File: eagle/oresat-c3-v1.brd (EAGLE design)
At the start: 99.8 x 94.7 mm, 174 parts, among them J1 J-SAMTEC-TFM-110-X1-XXX-D-RA, J10 U.FL, J11 U.FL, J13 U.FL, J14 U.FL, J15 HARWIN-2X8X1.27, J19 HARWIN-2X8X1.27, J2 U.FL, J3 U.FL, J4 U.FL, J6 J-SAMTEC-TFM-120-X1-XXX-D-RA, J7 FTSH-105-XX-X-DV-K, J8 U.FL, J9 U.FL, Q1 MOSFET-PCH-SOT23-6, U1 MAX892LEUA+T21-0036K-L, U11 U-ONSEMI-AX5043, U12 LP2985XX-N, U13 U-ONSEMI-AX5043, U14 LP2985XX-N, U2 TCAN330, U3 TCAN330, U4 TPS259621 - eFuse, U5 TPS62111RSA, U6 MAX6374KA-T21-0078H-L, U7 STM32F446RE, U9 SFEM016GB1EM1TO-A-HG-111-STD, X1 16MHZ-2.5x2mm, X3 TAITIEN-TY, X4 TAITIEN-TY

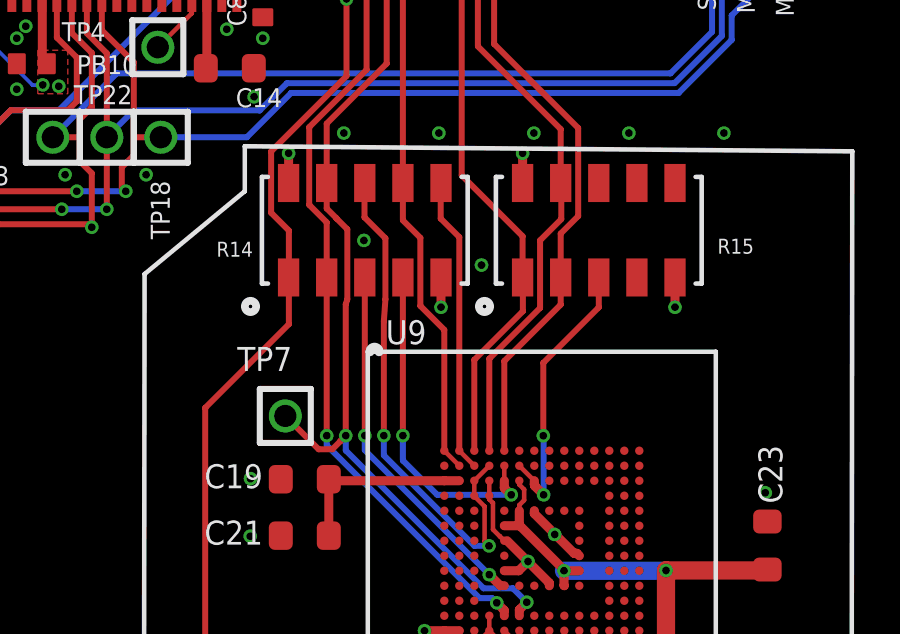
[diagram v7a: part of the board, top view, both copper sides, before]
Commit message: Fix net error
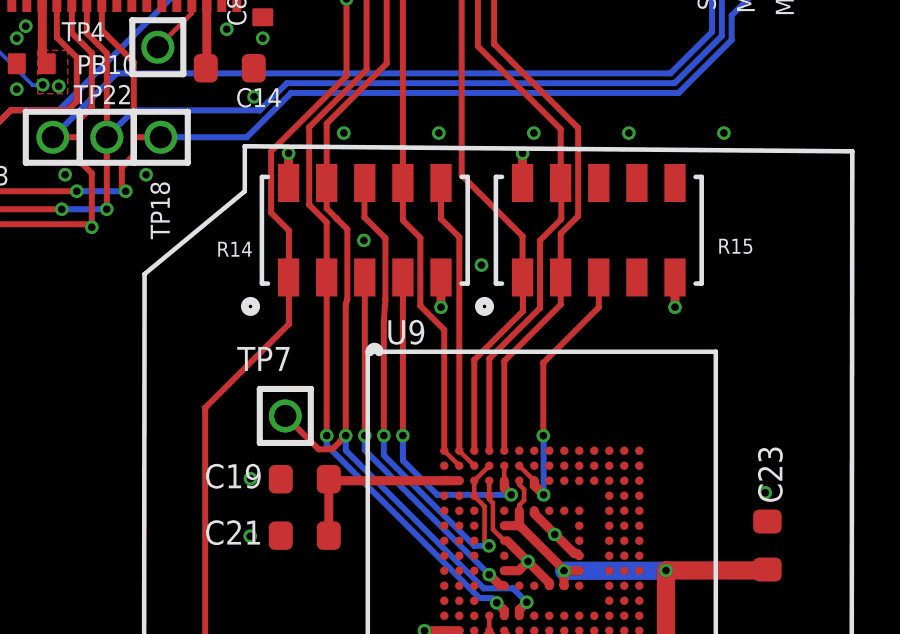
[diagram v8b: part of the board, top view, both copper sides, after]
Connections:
- removed net N$4: R14.6
- net SDIO_D4: now also R14.6
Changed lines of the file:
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@@
 <wire x1="89.000003125" y1="63.42999375" x2="89.8" y2="63.43" width="0" layer="19" extent="1-1"/>
 <wire x1="88.1" y1="58.88" x2="88.1" y2="60.28" width="0" layer="19" extent="1-1"/>
-<wire x1="84.8" y1="55.93" x2="88.1" y2="57.98" width="0" layer="19" extent="1-1"/>
-<wire x1="84.75" y1="55.88" x2="84.8" y2="55.93" width="0" layer="19" extent="1-1"/>
-<wire x1="82.3" y1="54.83" x2="83.7" y2="54.83" width="0" layer="19" extent="1-1"/>
-<wire x1="79.85" y1="56.38" x2="80.7" y2="55.98" width="0" layer="19" extent="1-1"/>
-<wire x1="79.85" y1="56.98" x2="79.85" y2="56.38" width="0" layer="19" extent="1-1"/>
-<wire x1="79.85" y1="57.58" x2="79.85" y2="56.98" width="0" layer="19" extent="1-1"/>
-<wire x1="79.85" y1="58.18" x2="79.85" y2="57.58" width="0" layer="19" extent="1-1"/>
-<wire x1="80.7" y1="58.18" x2="79.85" y2="58.18" width="0" layer="19" extent="1-1"/>
-<wire x1="80.7" y1="57.08" x2="79.85" y2="56.98" width="0" layer="19" extent="1-1"/>
-<wire x1="60.03" y1="55.85" x2="78.8" y2="56.98" width="0" layer="19" extent="1-1"/>
-<wire x1="59.95" y1="55.19" x2="60.03" y2="55.85" width="0" layer="19" extent="1-1"/>
-<wire x1="59.3" y1="55.2" x2="59.95" y2="55.19" width="0" layer="19" extent="1-1"/>
-<wire x1="59.585" y1="54.625" x2="59.3" y2="55.2" width="0" layer="19" extent="1-1"/>
-<wire x1="59.3" y1="55.9" x2="59.3" y2="55.2" width="0" layer="19" extent="1-1"/>
-<wire x1="58.6" y1="46" x2="59.585" y2="54.625" width="0" layer="19" extent="1-1"/>
-<wire x1="59.46" y1="39.7654" x2="58.674" y2="45.212" width="0" layer="19" extent="1-1"/>
-<wire x1="64.54" y1="35.6252" x2="59.46" y2="38.7748" width="0" layer="19" extent="1-1"/>
-<wire x1="67.26" y1="38.7748" x2="64.54" y2="35.6252" width="0" layer="19" extent="1-1"/>
-<wire x1="72.32" y1="35.64380625" x2="67.26" y2="38.7748" width="0" layer="19" extent="1-1"/>
-<wire x1="72.34" y1="35.6252" x2="72.332934375" y2="35.630871875" width="0" layer="19" extent="1-1"/>
-<wire x1="51.235" y1="45.275" x2="57.735" y2="45.275" width="0" layer="19" extent="1-1"/>
-<wire x1="51.265" y1="42.045" x2="51.4" y2="42.75" width="0" layer="19" extent="1-1"/>
-<wire x1="32.5" y1="65.1" x2="32.5" y2="65.6" width="0" layer="19" extent="1-1"/>
-<wire x1="32" y1="65.6" x2="32.5" y2="65.6" width="0" layer="19" extent="1-1"/>
-<wire x1="31.5" y1="65.6" x2="32" y2="65.6" width="0" layer="19" extent="1-1"/>
-<wire x1="31.5" y1="65.1" x2="31.5" y2="65.6" width="0" layer="19" extent="1-1"/>
-<wire x1="31" y1="65.1" x2="31.5" y2="65.1" width="0" layer="19" extent="1-1"/>
-<wire x1="31" y1="65.6" x2="31.5" y2="65.6" width="0" layer="19" extent="1-1"/>
-<wire x1="32" y1="65.1" x2="32.5" y2="65.1" width="0" layer="19" extent="1-1"/>
-<wire x1="51.8" y1="42" x2="51.265" y2="42.045" width="0" layer="19" extent="1-1"/>
-<wire x1="47.7" y1="55.5" x2="47.4" y2="54.864" width="0" layer="19" extent="1-1"/>
-<wire x1="48.385" y1="54.625" x2="47.4" y2="54.864" width="0" layer="19" extent="1-1"/>
-<wire x1="48.7" y1="55.2" x2="48.385" y2="54.625" width="0" layer="19" extent="1-1"/>
-<wire x1="32" y1="66.7" x2="32" y2="65.6" width="0" layer="19" extent="1-1"/>
-<wire x1="49.54" y1="56.16" x2="48.7" y2="55.2" width="0" layer="19" extent="1-1"/>
-<wire x1="50.235" y1="56.475" x2="49.54" y2="56.16" width="0" layer="19" extent="1-1"/>
-<wire x1="49.37" y1="57.05" x2="49.54" y2="56.16" width="0" layer="19" extent="1-1"/>
-<wire x1="49.911" y1="57.4" x2="49.37" y2="57.05" width="0" layer="19" extent="1-1"/>
-<wire x1="28.7" y1="65.425" x2="31" y2="65.1" width="0" layer="19" extent="1-1"/>
-<wire x1="26.725" y1="72.625" x2="28.7" y2="65.425" width="0" layer="19" extent="1-1"/>
-<wire x1="25.7" y1="72.65" x2="25.725" y2="72.625" width="0" layer="19" extent="1-1"/>
-<wire x1="21" y1="77.4" x2="25.7" y2="72.65" width="0" layer="19" extent="1-1"/>
-<wire x1="18.9" y1="72" x2="19.1" y2="77.4" width="0" layer="19" extent="1-1"/>
-<wire x1="57.5" y1="70.825" x2="50.4" y2="66.3" width="0" layer="19" extent="1-1"/>
-<wire x1="59.617" y1="70.912" x2="59.6" y2="70.9" width="0" layer="19" extent="1-1"/>
-<wire x1="61.07" y1="70.365" x2="59.617" y2="70.912" width="0" layer="19" extent="1-1"/>
-<wire x1="61.07" y1="70.364996875" x2="61.07" y2="70.365" width="0" layer="19" extent="1-1"/>
-<wire x1="10.2" y1="66.07" x2="18.9" y2="71.2" width="0" layer="19" extent="1-1"/>
-<wire x1="10.2" y1="63.53" x2="10.2" y2="66.07" width="0" layer="19" extent="1-1"/>
-<wire x1="56.7" y1="15.92" x2="64.54" y2="34.6346" width="0" layer="19" extent="1-1"/>
-<wire x1="38.905" y1="20.255" x2="56.7" y2="15.92" width="0" layer="19" extent="1-1"/>
-<wire x1="37.855" y1="20.855" x2="37.855" y2="20.255" width="0" layer="19" extent="1-1"/>
-<wire x1="37.855" y1="19.655" x2="37.855" y2="20.255" width="0" layer="19" extent="1-1"/>
-<wire x1="37.855" y1="19.055" x2="37.855" y2="19.655" width="0" layer="19" extent="1-1"/>
-<wire x1="37.005" y1="19.055" x2="37.855" y2="19.055" width="0" layer="19" extent="1-1"/>
-<wire x1="37.005" y1="20.155" x2="37.855" y2="20.255" width="0" layer="19" extent="1-1"/>
-<wire x1="37.005" y1="21.255" x2="37.855" y2="20.855" width="0" layer="19" extent="1-1"/>
-<wire x1="34.005" y1="22.405" x2="35.405" y2="22.405" width="0" layer="19" extent="1-1"/>
+<wire x1="61.07" y1="70.365" x2="61.07" y2="70.364996875" width="0" layer="19" extent="1-1"/>
+<wire x1="59.6" y1="70.9" x2="59.617" y2="70.912" width="0" layer="19" extent="1-1"/>
+<wire x1="72.332934375" y1="35.630871875" x2="72.34" y2="35.6252" width="0" layer="19" extent="1-1"/>
+<wire x1="25.725" y1="72.625" x2="25.7" y2="72.65" width="0" layer="19" extent="1-1"/>
+<wire x1="84.8" y1="55.93" x2="84.75" y2="55.88" width="0" layer="19" extent="1-1"/>
 <wire x1="32.905" y1="21.305" x2="32.955" y2="21.355" width="0" layer="19" extent="1-1"/>
-<wire x1="29.605" y1="19.255" x2="32.905" y2="21.305" width="0" layer="19" extent="1-1"/>
 <wire x1="29.605" y1="16.955" x2="29.605" y2="18.355" width="0" layer="19" extent="1-1"/>
 <wire x1="27.905" y1="13.805" x2="28.704996875" y2="13.805003125" width="0" layer="19" extent="1-1"/>
-<wire x1="21.082" y1="13.97" x2="27.905" y2="13.805" width="0" layer="19" extent="1-16"/>
+<wire x1="56.7" y1="15.92" x2="38.905" y2="20.255" width="0" layer="19" extent="1-1"/>
 </signal>
 <signal name="SDAOPT2">
@@
 <contactref element="U9" pad="A2"/>
 <contactref element="U9" pad="B3"/>
-<wire x1="65.15" y1="29.85" x2="65.15" y2="36.97" width="0.2" layer="1"/>
-<wire x1="65.15" y1="36.97" x2="64.53" y2="37.59" width="0.2" layer="1"/>
-<wire x1="64.53" y1="37.59" x2="64.53" y2="38.7648" width="0.2" layer="1"/>
+<wire x1="65.15" y1="36.97" x2="65.15" y2="29.85" width="0.2" layer="1"/>
+<contactref element="R14" pad="6"/>
+<wire x1="64.54" y1="38.7748" x2="64.54" y2="37.6" width="0.2" layer="1"/>
+<wire x1="64.54" y1="37.6" x2="64.53" y2="37.59" width="0.1524" layer="1"/>
+<wire x1="64.54" y1="37.6" x2="64.54" y2="37.58" width="0.2" layer="1"/>
+<wire x1="64.54" y1="37.58" x2="65.15" y2="36.97" width="0.2" layer="1"/>
 </signal>
 <signal name="SDIO_D5">
@@
 <wire x1="76.8" y1="68.545" x2="76.81" y2="68.545" width="0.39" layer="1"/>
 </signal>
-<signal name="N$4">
-<contactref element="R14" pad="6"/>
-</signal>
 </signals>
